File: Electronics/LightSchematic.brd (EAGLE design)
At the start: 68.6 x 35.2 mm, 7 parts, among them IC1 7805T, IC2 ATMEGA328-20P

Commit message: Add v0.2.0 board and schematic for milestone 4
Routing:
- net 5V: track 0.00 -> 44.7 mm
- net 9V: track 0.00 -> 37.7 mm
- net DIN: track 0.00 -> 22.3 mm
- net PWM: track 0.00 -> 16.8 mm
- net N$3: track 0.00 -> 3.00 mm
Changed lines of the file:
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@@
 </class>
 </classes>
-<designrules name="default">
+<designrules name="default *">
 <description language="de">&lt;b&gt;EAGLE Design Rules&lt;/b&gt;
 &lt;p&gt;
@@
 <contactref element="G1" pad="+"/>
 <contactref element="IC1" pad="1"/>
+<wire x1="62.23" y1="10.16" x2="59.69" y2="10.16" width="0.1524" layer="1"/>
+<wire x1="59.69" y1="10.16" x2="57.15" y2="12.7" width="0.1524" layer="1"/>
+<wire x1="57.15" y1="12.7" x2="57.15" y2="15.24" width="0.1524" layer="1"/>
+<wire x1="57.15" y1="15.24" x2="55.88" y2="16.51" width="0.1524" layer="1"/>
+<wire x1="55.88" y1="16.51" x2="35.56" y2="16.51" width="0.1524" layer="1"/>
+<wire x1="35.56" y1="16.51" x2="34.29" y2="15.24" width="0.1524" layer="1"/>
+<wire x1="34.29" y1="15.24" x2="34.29" y2="10.16" width="0.1524" layer="1"/>
 </signal>
 <signal name="N$3">
 <contactref element="R2" pad="1"/>
 <contactref element="D1" pad="A"/>
+<wire x1="55.88" y1="19.63" x2="55.88" y2="22.63" width="0.1524" layer="1"/>
 </signal>
 <signal name="5V">
@@
 <contactref element="IC2" pad="7"/>
 <contactref element="IC2" pad="20"/>
+<wire x1="18.288" y1="5.334" x2="26.416" y2="5.334" width="0.1524" layer="1"/>
+<wire x1="26.416" y1="5.334" x2="26.67" y2="5.08" width="0.1524" layer="1"/>
+<wire x1="26.67" y1="5.08" x2="34.29" y2="5.08" width="0.1524" layer="1"/>
+<wire x1="26.416" y1="5.334" x2="26.416" y2="17.526" width="0.1524" layer="1"/>
+<wire x1="29.21" y1="20.32" x2="29.21" y2="21.59" width="0.1524" layer="1"/>
+<wire x1="26.416" y1="17.526" x2="29.21" y2="20.32" width="0.1524" layer="1"/>
+<wire x1="29.21" y1="21.59" x2="29.21" y2="25.4" width="0.1524" layer="1"/>
+<wire x1="29.21" y1="25.4" x2="30.48" y2="26.67" width="0.1524" layer="1"/>
+<wire x1="30.48" y1="26.67" x2="33.02" y2="26.67" width="0.1524" layer="1"/>
+<wire x1="33.02" y1="26.67" x2="34.29" y2="27.94" width="0.1524" layer="1"/>
+<wire x1="34.29" y1="27.94" x2="34.29" y2="29.21" width="0.1524" layer="1"/>
 </signal>
 <signal name="GND">
@@
 <contactref element="S1" pad="P"/>
 <contactref element="IC2" pad="2"/>
+<wire x1="11.43" y1="18.36" x2="12.12" y2="19.05" width="0.1524" layer="1"/>
+<wire x1="12.12" y1="19.05" x2="13.97" y2="19.05" width="0.1524" layer="1"/>
+<wire x1="13.97" y1="19.05" x2="15.24" y2="20.32" width="0.1524" layer="1"/>
+<wire x1="15.24" y1="20.32" x2="15.24" y2="21.59" width="0.1524" layer="1"/>
+<wire x1="15.24" y1="21.59" x2="16.51" y2="21.59" width="0.1524" layer="1"/>
+<wire x1="13.97" y1="19.05" x2="15.24" y2="17.78" width="0.1524" layer="1"/>
+<wire x1="15.24" y1="17.78" x2="19.05" y2="17.78" width="0.1524" layer="1"/>
+<wire x1="19.05" y1="17.78" x2="21.59" y2="15.24" width="0.1524" layer="1"/>
+<wire x1="21.59" y1="15.24" x2="21.59" y2="12.7" width="0.1524" layer="1"/>
+<wire x1="21.59" y1="12.7" x2="18.542" y2="12.7" width="0.1524" layer="1"/>
+<wire x1="18.542" y1="12.7" x2="18.288" y2="12.446" width="0.1524" layer="1"/>
 </signal>
 <signal name="PWM">
 <contactref element="IC2" pad="12"/>
 <contactref element="R2" pad="2"/>
+<wire x1="55.88" y1="18.47" x2="42.49" y2="18.47" width="0.1524" layer="1"/>
+<wire x1="42.49" y1="18.47" x2="41.91" y2="19.05" width="0.1524" layer="1"/>
+<wire x1="41.91" y1="19.05" x2="41.91" y2="21.59" width="0.1524" layer="1"/>
 </signal>
 </signals>

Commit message: Add v0.2.1 for milestone 4 review
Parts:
- moved R2 17.8 mm to (38.1, 17.8), turned to 90 degrees
- moved IC2 8.03 mm to (22.9, 27.9)
- moved D1 7.18 mm to (50.8, 19.1)
- moved R1 5.68 mm to (6.35, 20.3)
- moved IC1 4.02 mm to (40.6, 8.89)
- moved G1 4.02 mm to (58.4, 8.89)
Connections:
- net DIN: now also IC2.4; no longer IC2.2
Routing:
- net N$3: track 3.00 -> 12.8 mm
- net PWM: track 16.8 -> 8.43 mm
- net 9V: track 37.7 -> 34.1 mm
- net 5V: track 44.7 -> 41.5 mm
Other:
- board size 68.6 x 35.2 mm -> 66 x 36.5 mm

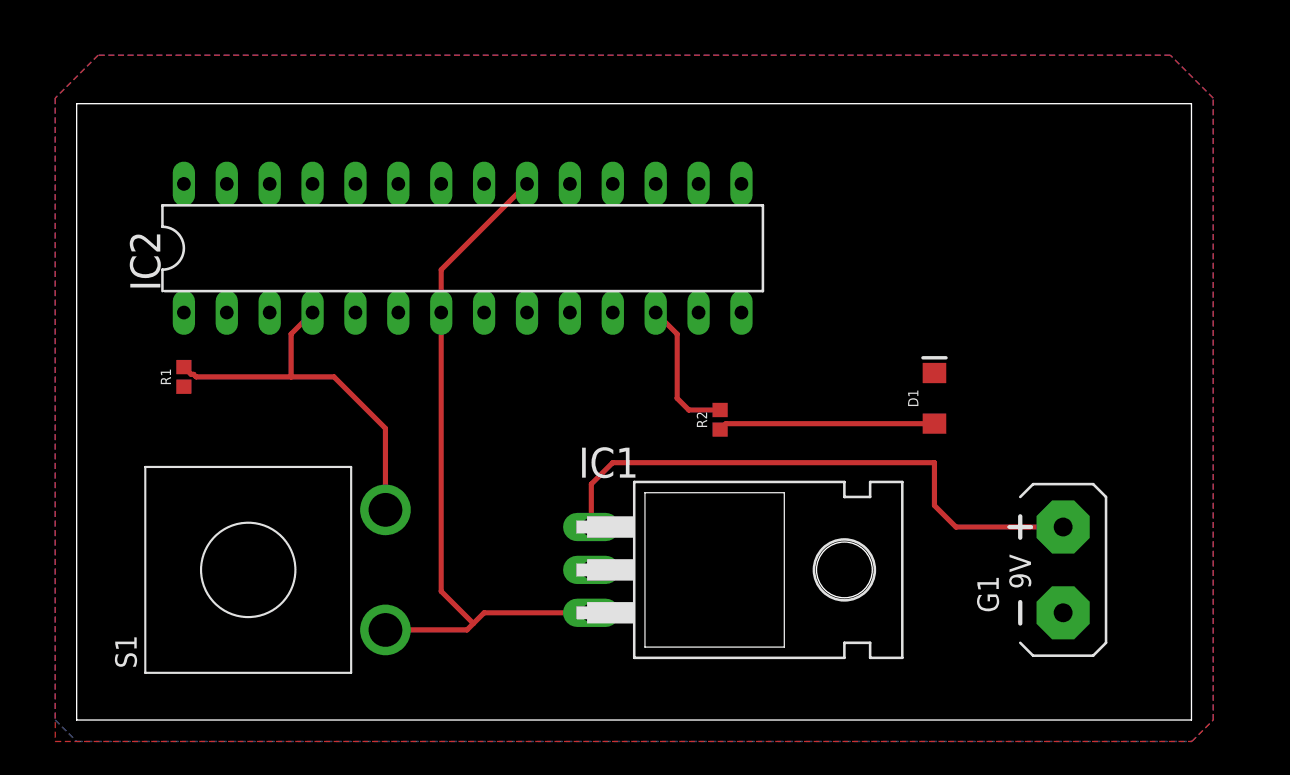
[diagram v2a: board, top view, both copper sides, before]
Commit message: Added holes to PCB
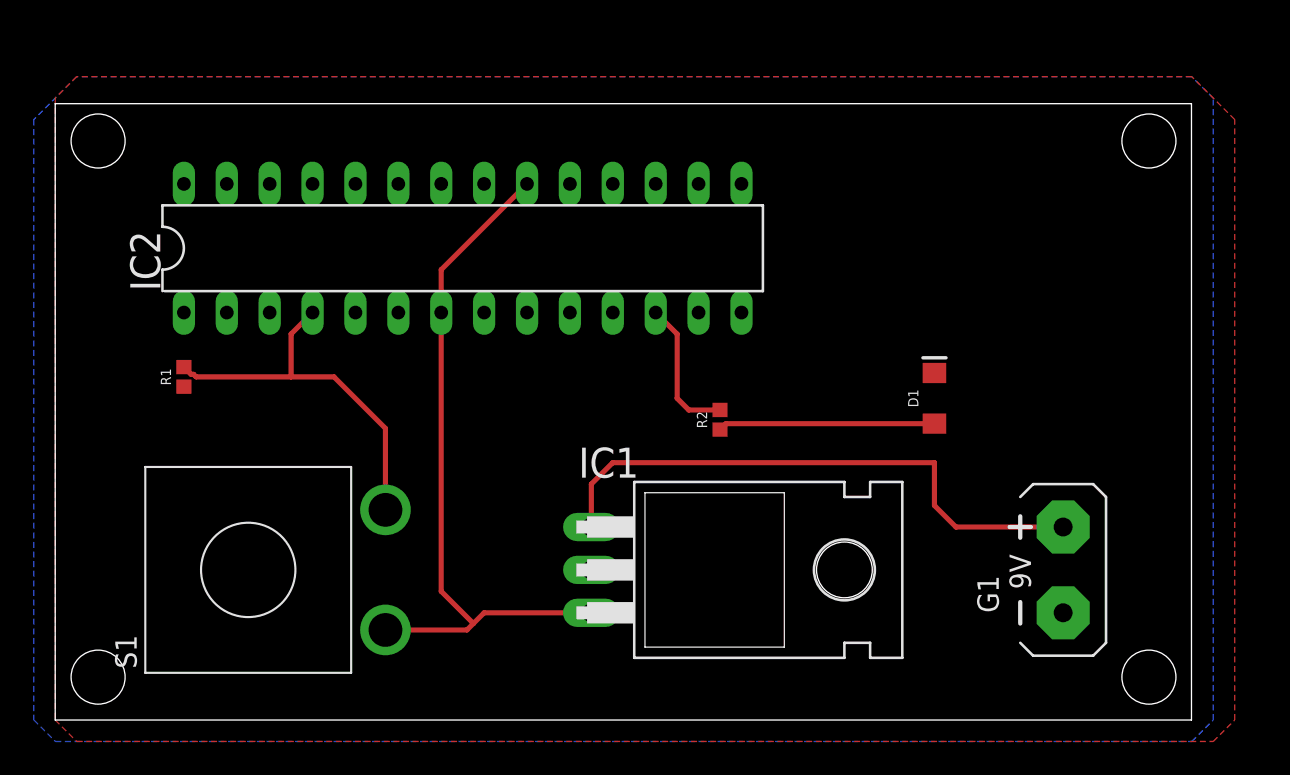
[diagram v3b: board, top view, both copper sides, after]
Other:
- board size 66 x 36.5 mm -> 67.3 x 36.5 mm
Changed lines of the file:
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@@
 <layer number="43" name="vRestrict" color="2" fill="10" visible="yes" active="yes"/>
 <layer number="44" name="Drills" color="7" fill="1" visible="no" active="yes"/>
-<layer number="45" name="Holes" color="7" fill="1" visible="no" active="yes"/>
+<layer number="45" name="Holes" color="7" fill="1" visible="yes" active="yes"/>
 <layer number="46" name="Milling" color="3" fill="1" visible="no" active="yes"/>
 <layer number="47" name="Measures" color="7" fill="1" visible="no" active="yes"/>
@@
 <board>
 <plain>
-<wire x1="0" y1="0" x2="66.02" y2="0" width="0" layer="20"/>
+<wire x1="-1.27" y1="0" x2="66.02" y2="0" width="0" layer="20"/>
 <wire x1="66.02" y1="0" x2="66.02" y2="36.5" width="0" layer="20"/>
-<wire x1="66.02" y1="36.5" x2="0" y2="36.5" width="0" layer="20"/>
-<wire x1="0" y1="36.5" x2="0" y2="0" width="0" layer="20"/>
+<wire x1="66.02" y1="36.5" x2="-1.27" y2="36.5" width="0" layer="20"/>
+<wire x1="-1.27" y1="36.5" x2="-1.27" y2="0" width="0" layer="20"/>
+<hole x="63.5" y="34.29" drill="3.199890625"/>
+<hole x="63.5" y="2.54" drill="3.199890625"/>
+<hole x="1.27" y="2.54" drill="3.199890625"/>
+<hole x="1.27" y="34.29" drill="3.199890625"/>
 </plain>
 <attributes>
@@
 <polygon width="0.1524" layer="1">
 <vertex x="-1.27" y="36.83"/>
+<vertex x="-1.27" y="0"/>
+<vertex x="0" y="-1.27"/>
+<vertex x="67.31" y="-1.27"/>
+<vertex x="68.58" y="0"/>
+<vertex x="68.58" y="35.56"/>
+<vertex x="66.04" y="38.1"/>
+<vertex x="0" y="38.1"/>
+</polygon>
+<polygon width="0.1524" layer="16">
+<vertex x="-2.54" y="35.56"/>
+<vertex x="-2.54" y="0"/>
 <vertex x="-1.27" y="-1.27"/>
 <vertex x="66.04" y="-1.27"/>
 <vertex x="67.31" y="0"/>
 <vertex x="67.31" y="36.83"/>
-<vertex x="64.77" y="39.37"/>
-<vertex x="1.27" y="39.37"/>
-</polygon>
-<polygon width="0.1524" layer="16">
-<vertex x="-1.27" y="36.83"/>
-<vertex x="-1.27" y="0"/>
-<vertex x="0" y="-1.27"/>
-<vertex x="66.04" y="-1.27"/>
-<vertex x="67.31" y="0"/>
-<vertex x="67.31" y="36.83"/>
-<vertex x="64.77" y="39.37"/>
-<vertex x="1.27" y="39.37"/>
+<vertex x="66.04" y="38.1"/>
+<vertex x="0" y="38.1"/>
 </polygon>
 </signal>

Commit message: Added 16 MHz crystal oscillator and 2 22 pF capacitors
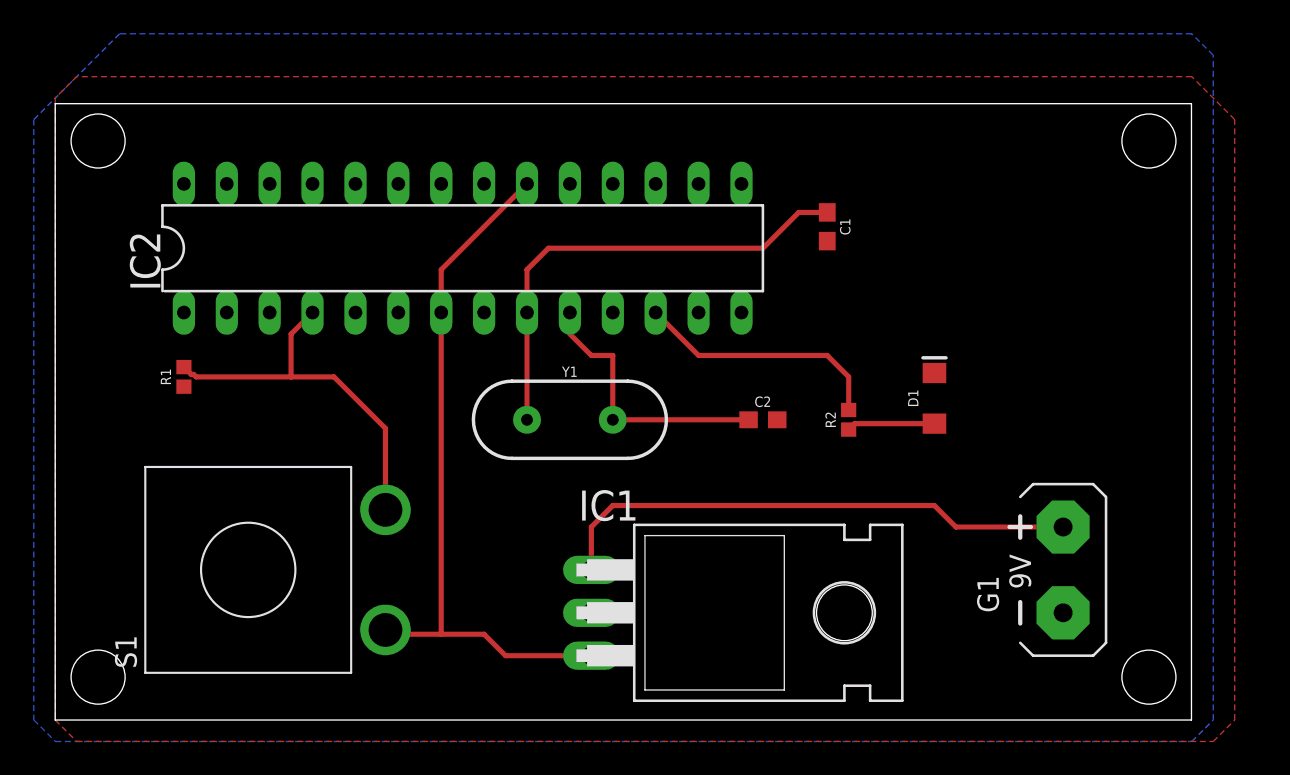
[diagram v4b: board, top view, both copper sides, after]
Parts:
- added C1, C2: 22pF, SparkFun-Capacitors:0603
- added Y1: 16MHz, SparkFun-Clocks:HC49US
- R1: value 100K -> 4.7k
- R2: value 100K -> 150
- moved R2 7.62 mm to (45.7, 17.8)
- moved IC1 2.54 mm to (40.6, 6.35)
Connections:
- new net N$1: C1.1, IC2.9, Y1.1
- new net N$2: C2.1, IC2.10, Y1.2
- net GND: now also C1.2, C2.2
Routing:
- net N$1: track 0.00 -> 28.1 mm
- net N$2: track 0.00 -> 16.2 mm
- net N$3: track 12.8 -> 5.22 mm
- net PWM: track 8.43 -> 15.0 mm
- net 9V: track 34.1 -> 31.5 mm

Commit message: Add files via upload
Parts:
- removed G1: AB9V, battery:AB9V
- added JP1: (no value), pinhead:1X02
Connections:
- net 9V: now also JP1.1; no longer G1.+
- net GND: now also JP1.2; no longer G1.-
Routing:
- net 9V: track 31.5 -> 33.9 mm
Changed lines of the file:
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@@
 <param name="mtCopper" value="0.035mm 0.035mm 0.035mm 0.035mm 0.035mm 0.035mm 0.035mm 0.035mm 0.035mm 0.035mm 0.035mm 0.035mm 0.035mm 0.035mm 0.035mm 0.035mm"/>
 <param name="mtIsolate" value="1.5mm 0.15mm 0.2mm 0.15mm 0.2mm 0.15mm 0.2mm 0.15mm 0.2mm 0.15mm 0.2mm 0.15mm 0.2mm 0.15mm 0.2mm"/>
-<param name="mdWireWire" value="12mil"/>
+<param name="mdWireWire" value="20mil"/>
 <param name="mdWirePad" value="6mil"/>
 <param name="mdWireVia" value="6mil"/>
@@
 <attribute name="VALUE" x="51.7525" y="19.05" size="0.6096" layer="27" font="vector" ratio="20" rot="R90" align="top-center"/>
 </element>
-<element name="G1" library="battery" library_urn="urn:adsk.eagle:library:109" package="AB9V" package3d_urn="urn:adsk.eagle:package:4600/1" value="AB9V" x="58.42" y="8.89">
-<attribute name="NAME" x="54.61" y="6.35" size="1.27" layer="25" ratio="10" rot="R90"/>
-<attribute name="VALUE" x="62.865" y="6.35" size="1.27" layer="27" ratio="10" rot="R90"/>
-</element>
 <element name="IC1" library="linear" library_urn="urn:adsk.eagle:library:262" package="TO220H" package3d_urn="urn:adsk.eagle:package:16414/1" value="7805T" x="40.64" y="6.35" rot="R270">
 <attribute name="NAME" x="29.718" y="11.811" size="1.778" layer="25" ratio="10"/>
@@
 <attribute name="VALUE" x="40.64" y="17.018" size="0.6096" layer="27" font="vector" ratio="20" align="top-center"/>
 </element>
+<element name="JP1" library="pinhead" library_urn="urn:adsk.eagle:library:325" package="1X02" package3d_urn="urn:adsk.eagle:package:22435/2" value="" x="59.69" y="10.16" rot="R90">
+<attribute name="NAME" x="57.8612" y="7.5438" size="1.27" layer="25" ratio="10" rot="R90"/>
+<attribute name="VALUE" x="62.865" y="7.62" size="1.27" layer="27" rot="R90"/>
+</element>
 </elements>
 <signals>
 <signal name="9V">
-<contactref element="G1" pad="+"/>
 <contactref element="IC1" pad="1"/>
-<wire x1="58.42" y1="11.43" x2="52.07" y2="11.43" width="0.3048" layer="1"/>
-<wire x1="52.07" y1="11.43" x2="50.8" y2="12.7" width="0.3048" layer="1"/>
-<wire x1="50.8" y1="12.7" x2="31.75" y2="12.7" width="0.3048" layer="1"/>
+<wire x1="31.75" y1="12.7" x2="50.8" y2="12.7" width="0.3048" layer="1"/>
 <wire x1="31.75" y1="12.7" x2="30.48" y2="11.43" width="0.3048" layer="1"/>
 <wire x1="30.48" y1="11.43" x2="30.48" y2="8.89" width="0.3048" layer="1"/>
+<contactref element="JP1" pad="1"/>
+<wire x1="54.61" y1="8.89" x2="59.69" y2="8.89" width="0.3048" layer="1"/>
+<wire x1="50.8" y1="12.7" x2="54.61" y2="8.89" width="0.3048" layer="1"/>
 </signal>
 <signal name="N$3">
@@
 </signal>
 <signal name="GND">
-<contactref element="G1" pad="-"/>
 <contactref element="IC1" pad="2"/>
 <contactref element="IC2" pad="8"/>
@@
 <contactref element="C1" pad="2"/>
 <contactref element="C2" pad="2"/>
+<contactref element="JP1" pad="2"/>
 </signal>
 <signal name="DIN">
